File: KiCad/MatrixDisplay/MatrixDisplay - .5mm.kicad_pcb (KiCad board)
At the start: 2 copper layers, 3 parts, among them J1 PUT_IN, J2 Power, U1 mini_esp32

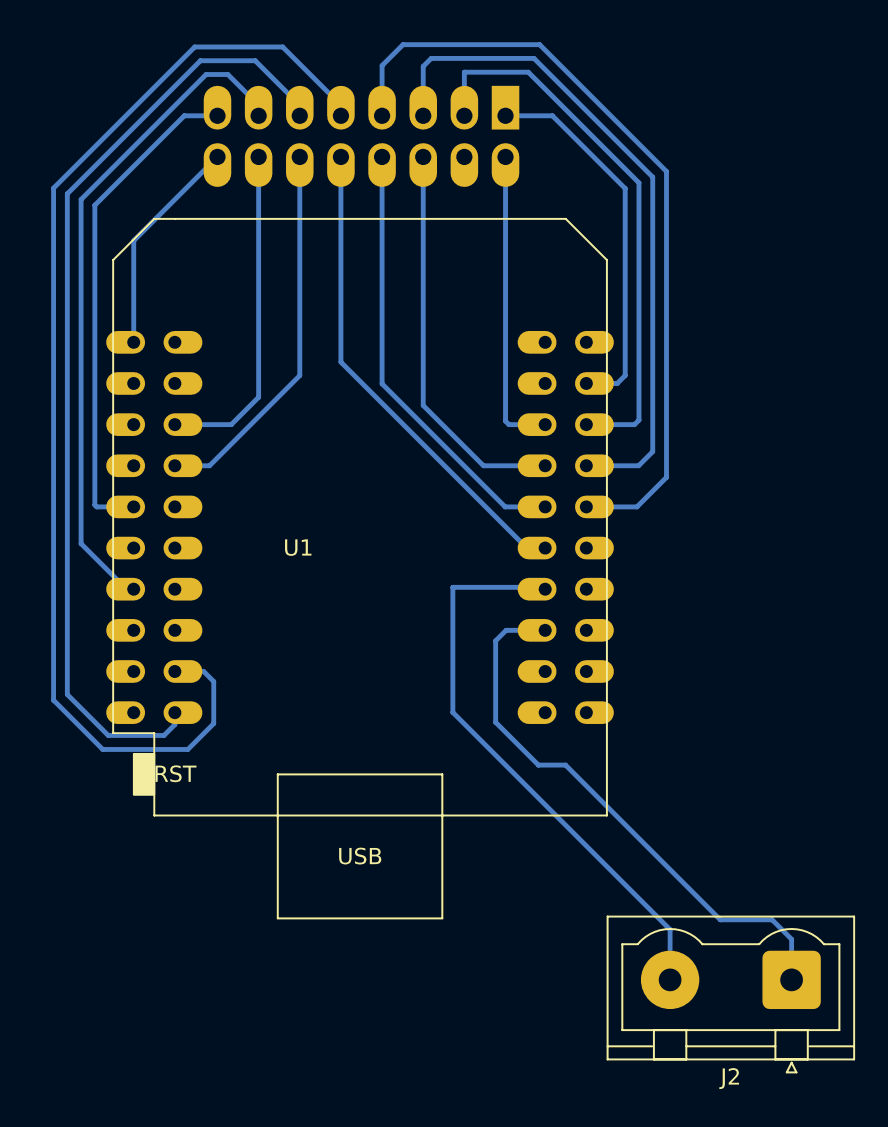
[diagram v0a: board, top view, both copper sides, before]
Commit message: add wifi setup instructins to display
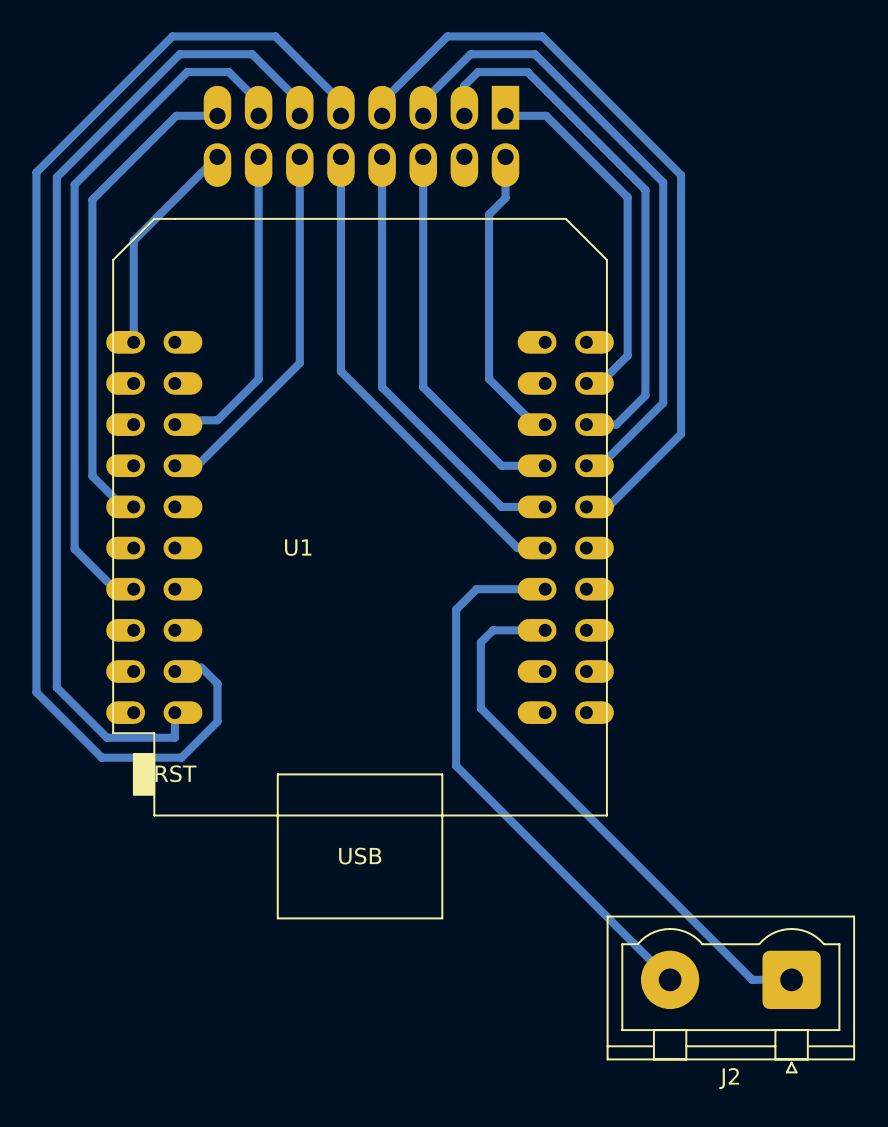
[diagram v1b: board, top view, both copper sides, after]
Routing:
- net Net-(U1-Pad20): track 59.2 -> 61.8 mm
- net Net-(U1-Pad18): track 72.2 -> 74.5 mm
- net Net-(U1-Pad13): track 41.3 -> 43.0 mm
- net Net-(J1-Pad5): track 41.9 -> 40.1 mm
- net Net-(J1-Pad16): track 49.1 -> 47.9 mm
- net Net-(J1-Pad3): track 34.3 -> 33.5 mm
- net Net-(J1-Pad7): track 49.0 -> 48.2 mm
- net Net-(J1-Pad14): track 20.7 -> 20.0 mm
- net Net-(J1-Pad6): track 24.4 -> 23.8 mm
- net Net-(U1-Pad9): track 30.8 -> 30.3 mm
